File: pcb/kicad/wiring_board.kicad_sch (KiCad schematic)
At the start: 7 parts, among them J1 2604-1106, J2 5V out

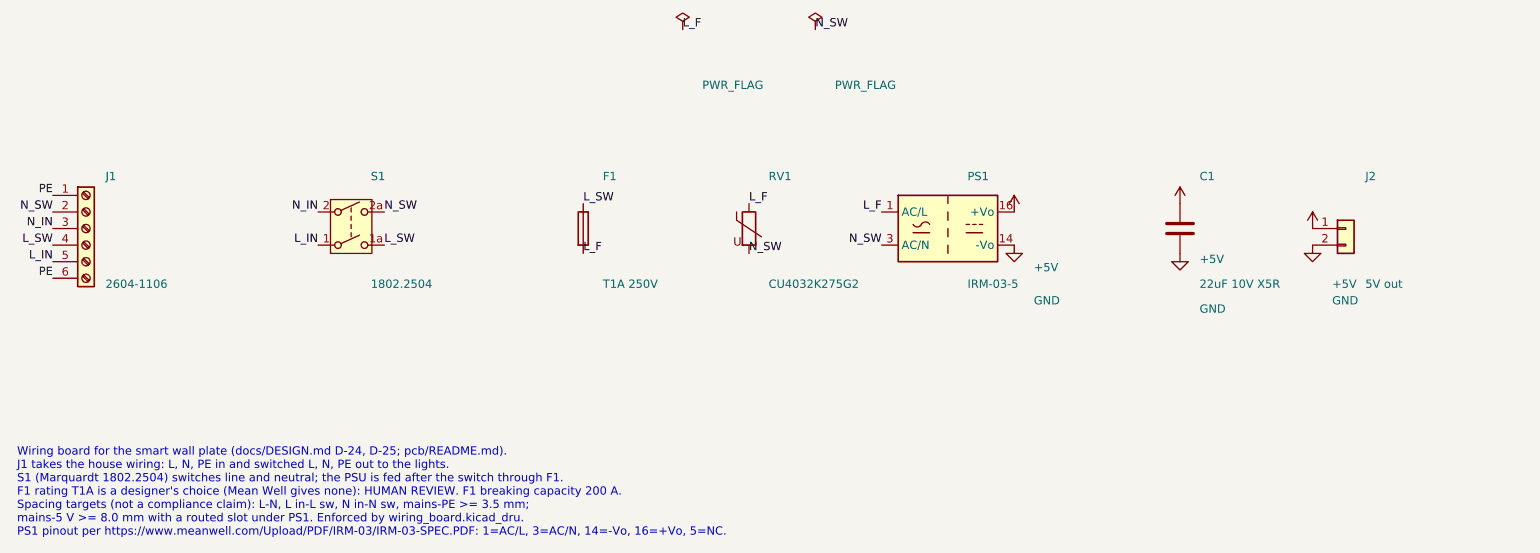
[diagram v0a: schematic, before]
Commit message: Wiring board: J1 and rocker from vendor models, rocker clear of WAGO pins, LOAD labels
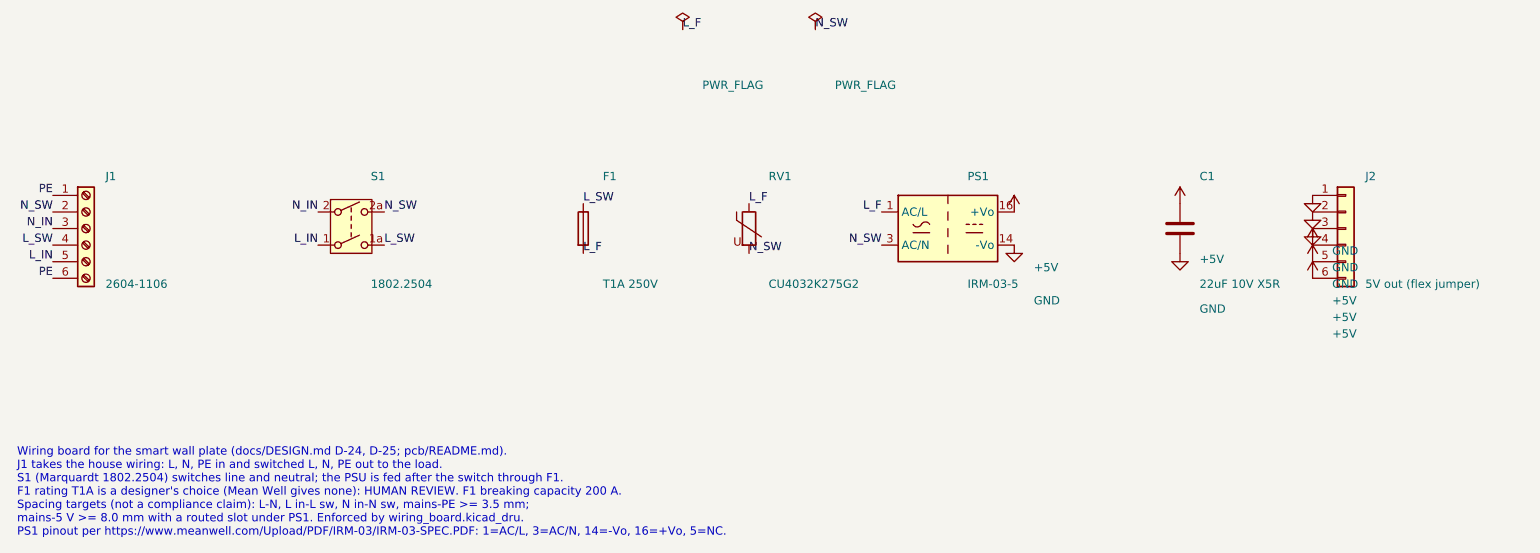
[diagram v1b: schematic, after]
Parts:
- J2: value 5V out -> 5V out (flex jumper); footprint wiring_board:JST_PH_S2B-PH-SM4-TB_1x02-1MP_P2.00mm_Horizontal -> wiring_board:Hirose_FH12-6S-0.5SH_1x06-1MP_P0.50mm_Horizontal; symbol wiring_board:Conn_01x02 -> wiring_board:Conn_01x06; MPN S2B-PH-SM4-TB(LF)(SN) -> FH12-6S-0.5SH(55); Manufacturer JST -> Hirose
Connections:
- net +5V: now also J2.4 (Pin_4), J2.5 (Pin_5), J2.6 (Pin_6); no longer J2.1 (Pin_1)
- net GND: now also J2.1 (Pin_1), J2.3 (Pin_3)
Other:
- note added: "Wiring board for the smart wall plate (docs/DESIGN.md D-24, D-25; pcb/README.md). J1 takes the house wiring: L, N, PE in and switched L, N, PE out to the load. S1 (Marquardt 1802.2504) switches line and neutral; the PSU is fed after the switch through F1. F1 rating T1A is a designer's choice (Mean Well gives none): HUMAN REVIEW. F1 breaking capacity 200 A. Spacing targets (not a compliance claim)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"
- note removed: "Wiring board for the smart wall plate (docs/DESIGN.md D-24, D-25; pcb/README.md). J1 takes the house wiring: L, N, PE in and switched L, N, PE out to the lights. S1 (Marquardt 1802.2504) switches line and neutral; the PSU is fed after the switch through F1. F1 rating T1A is a designer's choice (Mean Well gives none): HUMAN REVIEW. F1 breaking capacity 200 A. Spacing targets (not a compliance clai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"
